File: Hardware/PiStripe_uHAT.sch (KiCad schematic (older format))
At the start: 39 parts, among them J1 +12V, J2 LED, J3 IRRX, J4 RPi_GPIO, Q1 DMG2305UX-13, Q2 IRF8721PBF-1, Q3 IRF8721PBF-1, Q4 IRF8721PBF-1, U1 TPS54202, U2 DMMT5401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

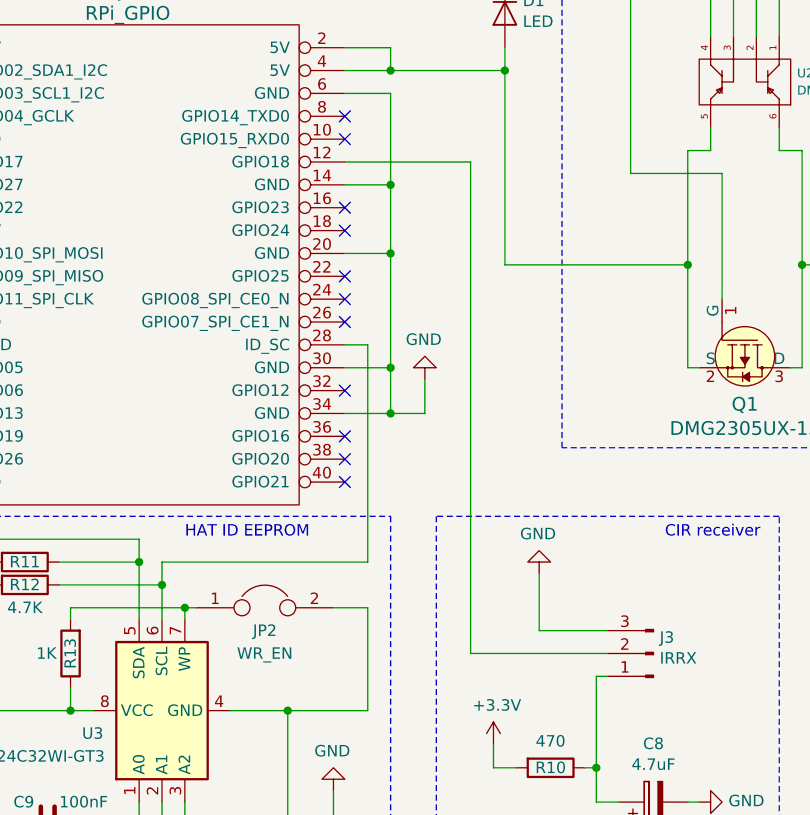
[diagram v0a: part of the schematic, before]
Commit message: v0.4: Change GPIO for IRRX from Pin 12 (GPIO18) to 22 (GPIO25)
Pin 12/GPIO18 is used by the phatDAC HAT which I want to combine with my
PiStripe uHAT.
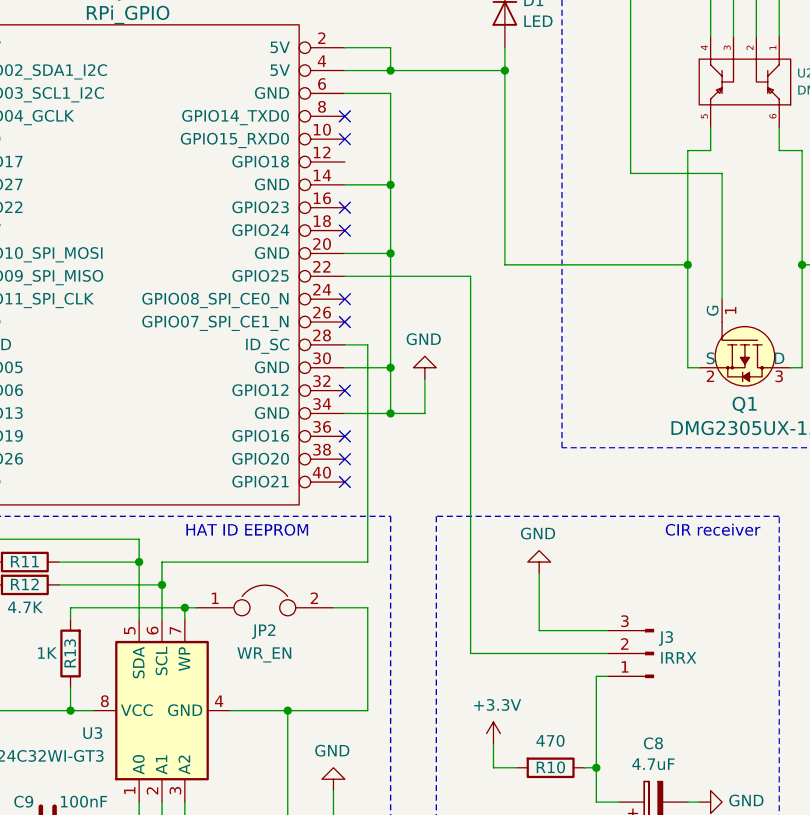
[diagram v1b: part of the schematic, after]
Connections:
- net at J4.12 (GPIO18): no longer J3.2 (Pin_2)
- net at J4.22 (GPIO25): now also J3.2 (Pin_2)
- no-connect marks 22 -> 21
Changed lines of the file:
@@
 EESchema Schematic File Version 4
+LIBS:PiStripe_uHAT-cache
 EELAYER 26 0
 EELAYER END
@@
 Sheet 1 1
 Title "PiStripe_uHAT"
-Date "2018-12-20"
-Rev ""
+Date "2018-12-24"
+Rev "0.4"
 Comp ""
 Comment1 ""
@@
 NoConn ~ 8600 3400
 NoConn ~ 8600 3500
-NoConn ~ 8600 3700
 NoConn ~ 8600 3800
 NoConn ~ 8600 3900
@@
 	8800 2800 9300 2800
 Connection ~ 9300 2800
-Wire Wire Line
-	8600 3200 9150 3200
 $Comp
 L power:GND #PWR013
@@
 	6800 5600 6800 6100
 Wire Wire Line
-	9150 3200 9150 5350
-Wire Wire Line
 	9300 2800 9300 3650
 $Comp
@@
 Wire Wire Line
 	5050 6300 5500 6300
+Wire Wire Line
+	8600 3700 9150 3700
+Wire Wire Line
+	9150 3700 9150 5350
 $EndSCHEMATC

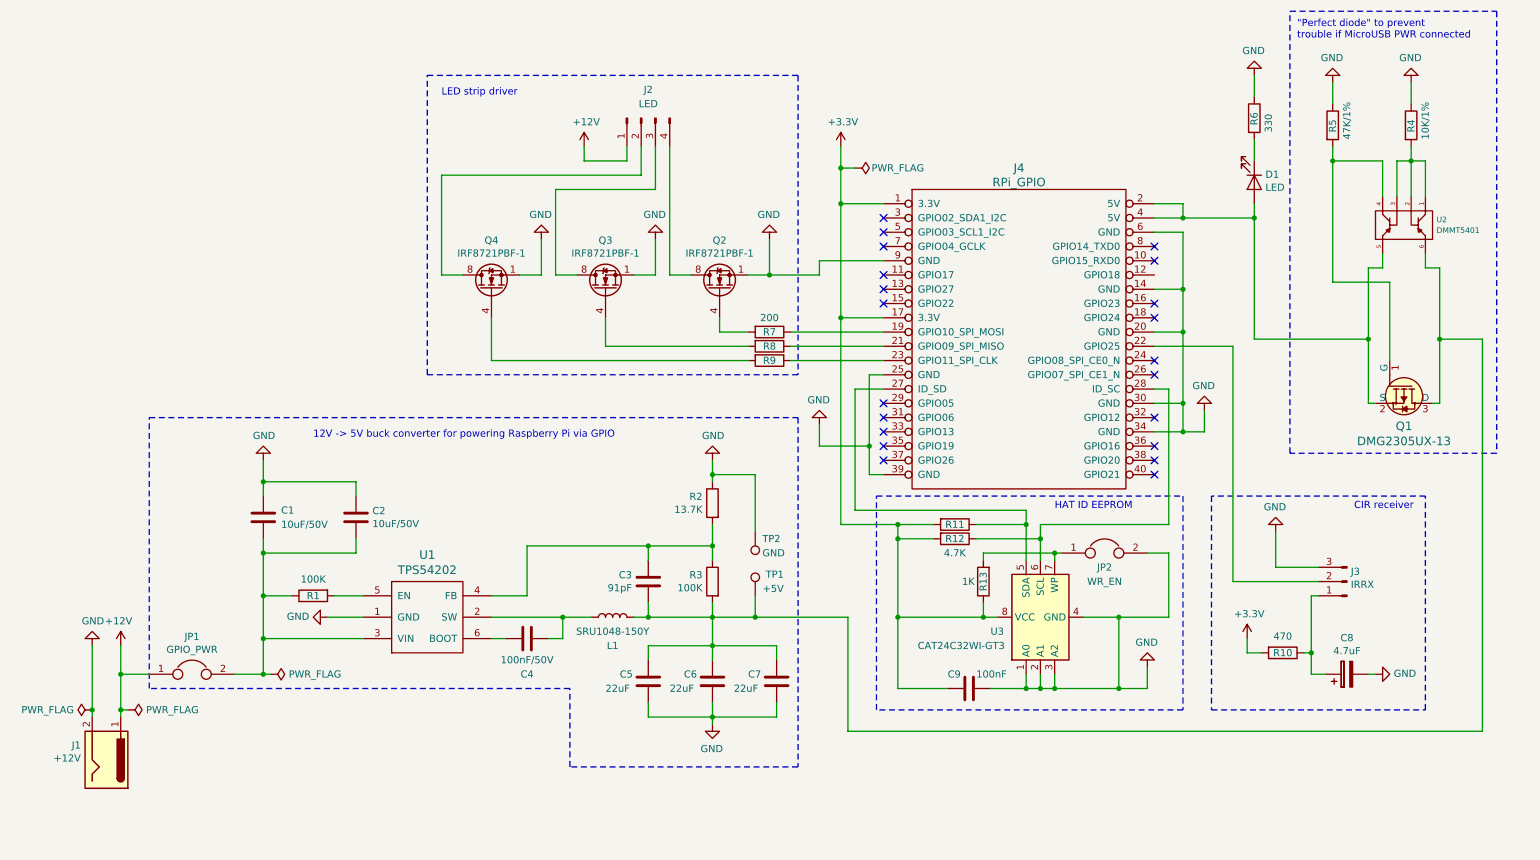
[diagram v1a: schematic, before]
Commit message: Turn GND arrows down in schematic
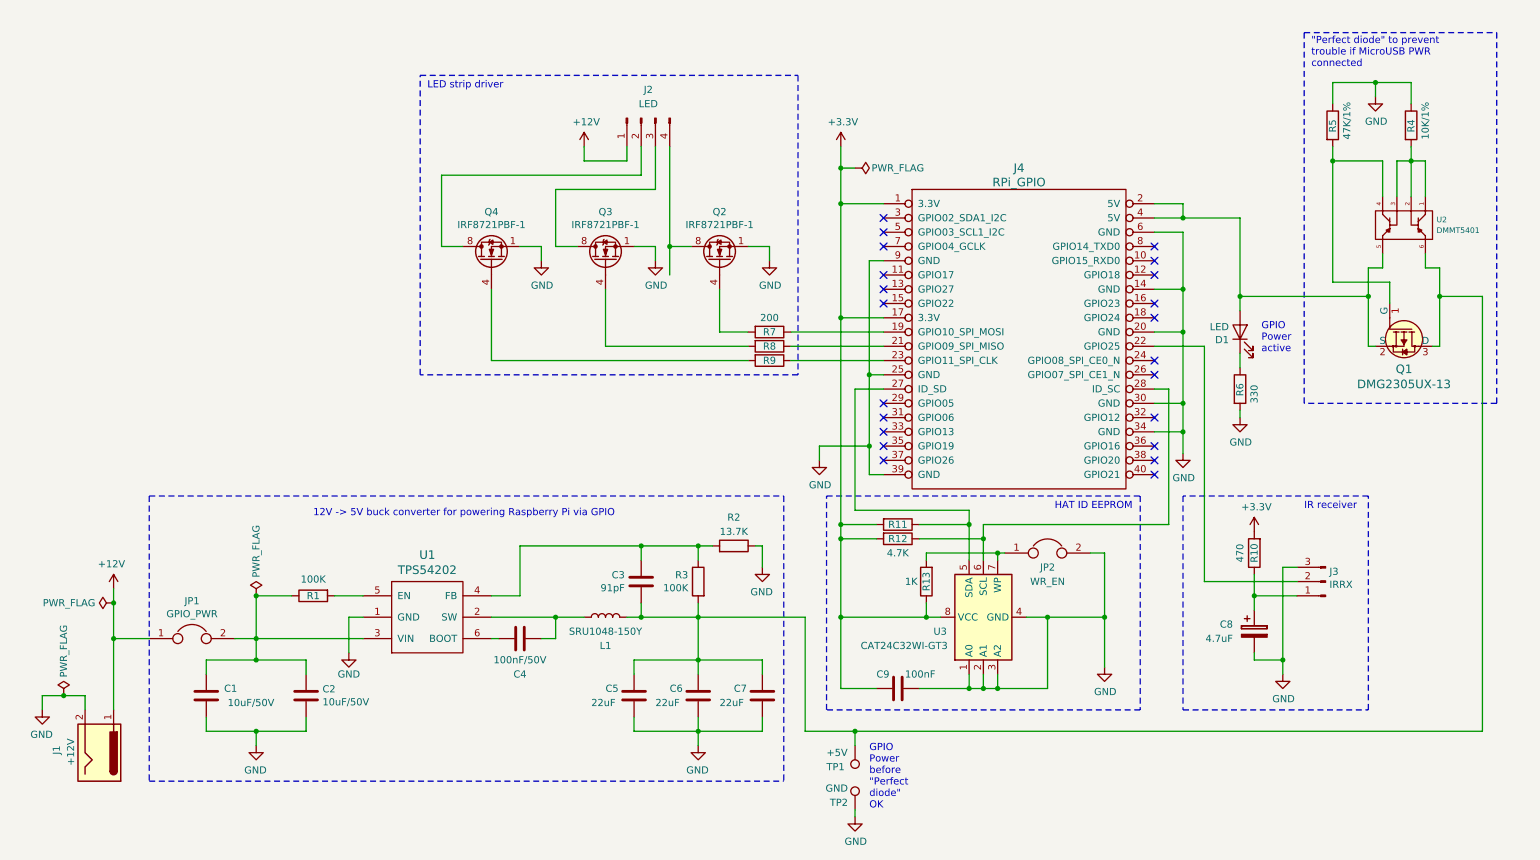
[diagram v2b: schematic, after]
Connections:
- net GND: now also C1.2, C2.2, R6.2; no longer C1.1, C2.1, R6.1
- net at D1.1 (K): now also R6.1; no longer R6.2
- net at JP1.2, R1.1, U1.3 (VIN): now also C1.1, C2.1; no longer C1.2, C2.2
- no-connect marks 21 -> 22
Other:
- note added: ""Perfect diode" to prevent\ntrouble if MicroUSB PWR\nconnected"
- note added: "GPIO\nPower\nactive"
- note added: "GPIO\nPower\nbefore\n"Perfect\ndiode"\nOK"
- note added: "IR receiver"
- note removed: ""Perfect diode" to prevent\ntrouble if MicroUSB PWR connected"
- note removed: "CIR receiver"
- moved on the sheet: C1, C2, C3, C4, C5, C6, C7, C8, C9, D1, J1, J3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

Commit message: Schematic: Tidy up IR receiver section
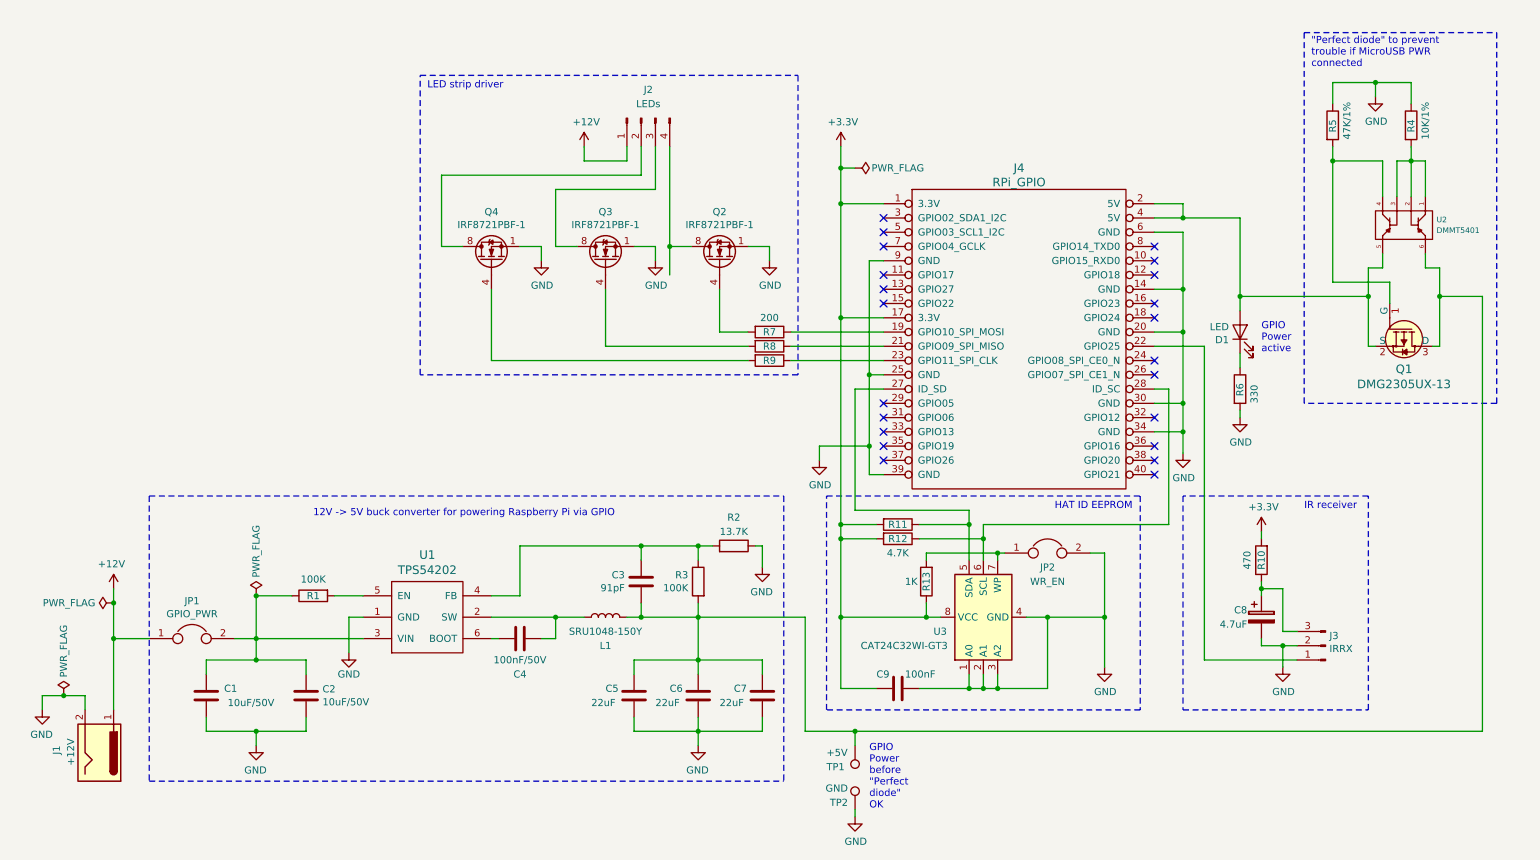
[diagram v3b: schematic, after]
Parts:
- J2: value LED -> LEDs
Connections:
- net GND: now also J3.2 (Pin_2); no longer J3.3 (Pin_3)
- net at J4.22 (GPIO25): now also J3.1 (Pin_1); no longer J3.2 (Pin_2)
- net at C8.1, R10.1: now also J3.3 (Pin_3); no longer J3.1 (Pin_1)
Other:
- moved on the sheet: C8, J3, R10
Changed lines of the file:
@@
 P 5000 2100
 F 0 "J2" V 4800 2050 50  0000 C CNN
-F 1 "LED" V 4900 2050 50  0000 C CNN
+F 1 "LEDs" V 4900 2050 50  0000 C CNN
 F 2 "Connector_PinHeader_1.27mm:PinHeader_1x04_P1.27mm_Horizontal" H 5000 2100 50  0001 C CNN
 F 3 "~" H 5000 2100 50  0001 C CNN
@@
 L power:+3.3V #PWR011
 U 1 1 5C1654B6
-P 9300 5000
-F 0 "#PWR011" H 9300 4850 50  0001 C CNN
-F 1 "+3.3V" H 9315 5173 50  0000 C CNN
-F 2 "" H 9300 5000 50  0001 C CNN
-F 3 "" H 9300 5000 50  0001 C CNN
-	1    9300 5000
+P 9350 5000
+F 0 "#PWR011" H 9350 4850 50  0001 C CNN
+F 1 "+3.3V" H 9365 5173 50  0000 C CNN
+F 2 "" H 9350 5000 50  0001 C CNN
+F 3 "" H 9350 5000 50  0001 C CNN
+	1    9350 5000
 	1    0    0    -1
 $EndComp
@@
 L Connector:Conn_01x03_Male J3
 U 1 1 5C214AA4
-P 9800 5350
-F 0 "J3" H 9773 5280 50  0000 R CNN
-F 1 "IRRX" H 9773 5371 50  0000 R CNN
-F 2 "Connector_PinHeader_1.27mm:PinHeader_1x03_P1.27mm_Horizontal" H 9800 5350 50  0001 C CNN
-F 3 "~" H 9800 5350 50  0001 C CNN
-	1    9800 5350
+P 9800 5800
+F 0 "J3" H 9773 5730 50  0000 R CNN
+F 1 "IRRX" H 9773 5821 50  0000 R CNN
+F 2 "Connector_PinHeader_1.27mm:PinHeader_1x03_P1.27mm_Horizontal" H 9800 5800 50  0001 C CNN
+F 3 "~" H 9800 5800 50  0001 C CNN
+	1    9800 5800
 	-1   0    0    1
 $EndComp
@@
 $EndComp
 Wire Wire Line
-	8950 5350 9600 5350
-Wire Wire Line
 	8600 4000 8700 4000
 Wire Wire Line
@@
 L Device:CP C8
 U 1 1 5C1DDE21
-P 9300 5700
-F 0 "C8" H 9150 5750 50  0000 R CNN
-F 1 "4.7uF" H 9150 5650 50  0000 R CNN
-F 2 "Capacitor_SMD:CP_Elec_4x5.8" H 9338 5550 50  0001 C CNN
-F 3 "~" H 9300 5700 50  0001 C CNN
-	1    9300 5700
+P 9350 5600
+F 0 "C8" H 9250 5650 50  0000 R CNN
+F 1 "4.7uF" H 9250 5550 50  0000 R CNN
+F 2 "Capacitor_SMD:CP_Elec_4x5.8" H 9388 5450 50  0001 C CNN
+F 3 "~" H 9350 5600 50  0001 C CNN
+	1    9350 5600
 	1    0    0    -1
 $EndComp
@@
 Wire Wire Line
 	8600 3700 8950 3700
-Wire Wire Line
-	9300 5450 9300 5300
-Wire Wire Line
-	9300 5450 9600 5450
-Wire Wire Line
-	9300 5550 9300 5450
-Connection ~ 9300 5450
 $Comp
 L power:GND #PWR0106
 U 1 1 5C33D48C
-P 9500 6000
-F 0 "#PWR0106" H 9500 5750 50  0001 C CNN
-F 1 "GND" H 9505 5827 50  0000 C CNN
-F 2 "" H 9500 6000 50  0001 C CNN
-F 3 "" H 9500 6000 50  0001 C CNN
-	1    9500 6000
-	1    0    0    -1
-$EndComp
-Wire Wire Line
-	9500 5250 9500 5900
-Wire Wire Line
-	9500 5250 9600 5250
-Wire Wire Line
-	9300 5850 9300 5900
-Wire Wire Line
-	9300 5900 9500 5900
-Connection ~ 9500 5900
-Wire Wire Line
-	9500 5900 9500 6000
+P 9500 5950
+F 0 "#PWR0106" H 9500 5700 50  0001 C CNN
+F 1 "GND" H 9505 5777 50  0000 C CNN
+F 2 "" H 9500 5950 50  0001 C CNN
+F 3 "" H 9500 5950 50  0001 C CNN
+	1    9500 5950
+	1    0    0    -1
+$EndComp
 Wire Wire Line
 	6250 4400 6250 4500
@@
 Wire Wire Line
 	9200 4150 9200 4200
-Wire Wire Line
-	8950 3700 8950 5350
 $Comp
 L Device:R R10
 U 1 1 5C15FAC5
-P 9300 5150
-F 0 "R10" V 9300 5150 50  0000 C CNN
-F 1 "470" V 9400 5150 50  0000 C CNN
-F 2 "Resistor_SMD:R_0805_2012Metric_Pad1.15x1.40mm_HandSolder" V 9230 5150 50  0001 C CNN
-F 3 "~" H 9300 5150 50  0001 C CNN
-	1    9300 5150
+P 9350 5200
+F 0 "R10" V 9350 5200 50  0000 C CNN
+F 1 "470" V 9450 5200 50  0000 C CNN
+F 2 "Resistor_SMD:R_0805_2012Metric_Pad1.15x1.40mm_HandSolder" V 9280 5200 50  0001 C CNN
+F 3 "~" H 9350 5200 50  0001 C CNN
+	1    9350 5200
 	-1   0    0    1
 $EndComp
@@
 	1    0    0    -1
 $EndComp
+Wire Wire Line
+	9500 5900 8950 5900
+Wire Wire Line
+	8950 3700 8950 5900
+Wire Wire Line
+	9500 5900 9600 5900
+Wire Wire Line
+	9500 5800 9600 5800
+Connection ~ 9500 5800
+Wire Wire Line
+	9500 5800 9500 5950
+Wire Wire Line
+	9350 5750 9350 5800
+Wire Wire Line
+	9350 5800 9500 5800
+Wire Wire Line
+	9350 5000 9350 5050
+Wire Wire Line
+	9350 5350 9350 5400
+Wire Wire Line
+	9350 5400 9500 5400
+Wire Wire Line
+	9500 5400 9500 5700
+Wire Wire Line
+	9500 5700 9600 5700
+Connection ~ 9350 5400
+Wire Wire Line
+	9350 5400 9350 5450
 $EndSCHEMATC
